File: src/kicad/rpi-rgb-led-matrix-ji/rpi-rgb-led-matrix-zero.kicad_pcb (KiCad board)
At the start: 2 copper layers, 65 x 30 mm, 11 parts, among them J1 Conn_01x02_Male, J2 Conn_02x10_Odd_Even, P1 Raspberry_Pi_2_3

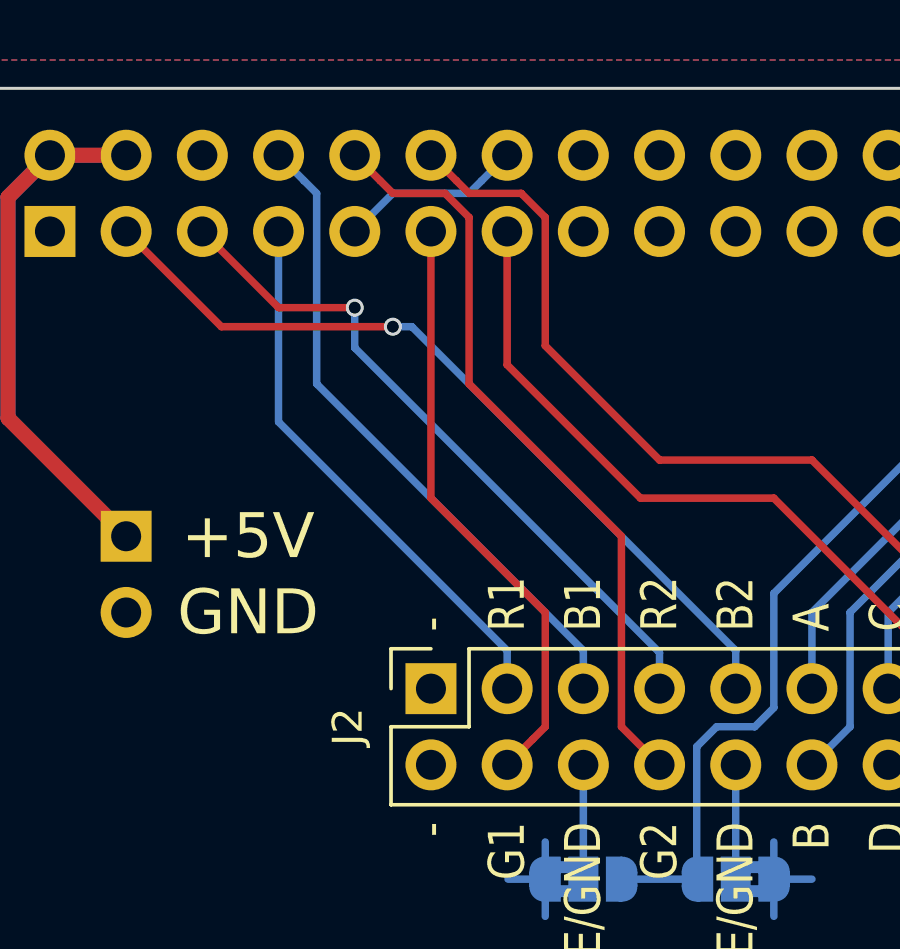
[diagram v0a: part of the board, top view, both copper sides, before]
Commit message: fixed g1/g2 inversion, removed virtual diode bypass
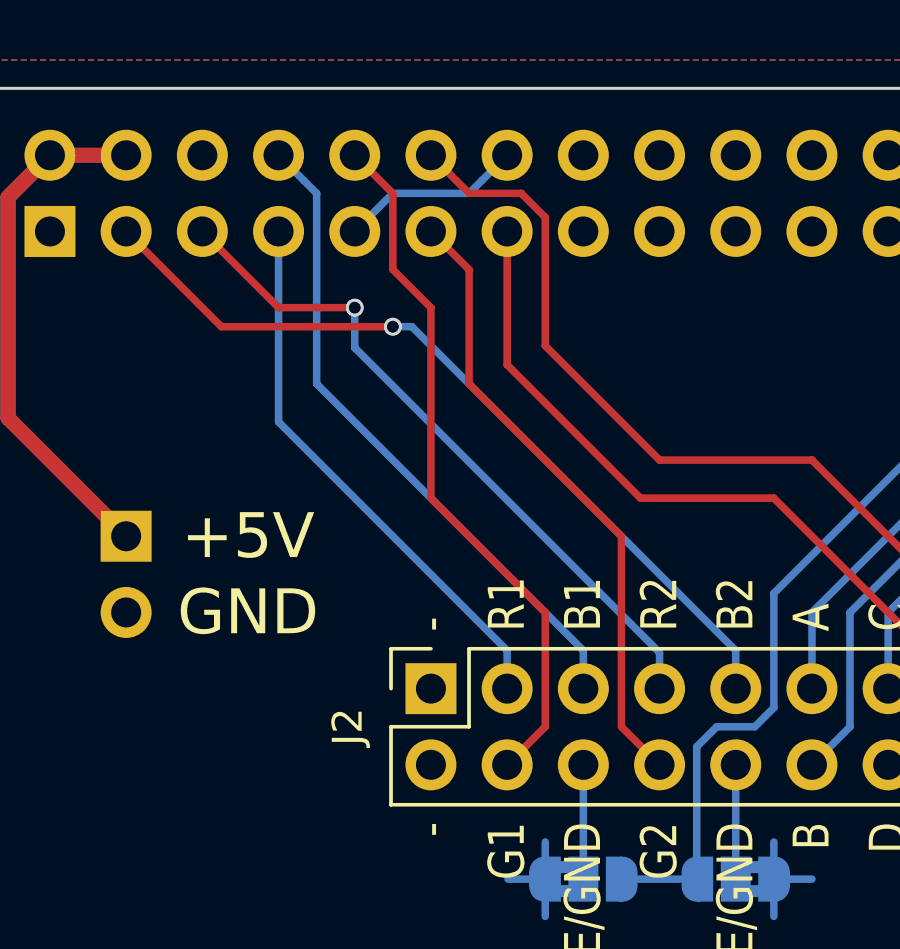
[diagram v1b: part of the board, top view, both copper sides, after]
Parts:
- H1, H2: value Power cable tie-down -> MountingHole
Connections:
- P1 pad 10: /G2_1 -> /G1_1
- P1 pad 11: /G1_1 -> /G2_1
- P1 pad 21: /G1_2 -> /G2_2
- P1 pad 22: /G2_2 -> /G1_2
- P1 pad 31: /G1_3 -> /G2_3
- P1 pad 32: /G2_3 -> /G1_3
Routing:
- net /G2_1: track 25.5 -> 20.9 mm
- net /G1_1: track 19.9 -> 23.5 mm
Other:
- board text added: "v1.2.3 20190324"
- board text removed: "v1.2 20190313"
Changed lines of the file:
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@@
     (thickness 1.6)
     (drawings 41)
-    (tracks 111)
+    (tracks 110)
     (zones 0)
     (modules 11)
@@
       (net 29 /E))
     (pad 32 thru_hole oval (at -2.54 -38.1 270) (size 1.7 1.7) (drill 1) (layers *.Cu *.Mask)
+      (net 30 /G1_3))
+    (pad 31 thru_hole oval (at 0 -38.1 270) (size 1.7 1.7) (drill 1) (layers *.Cu *.Mask)
       (net 28 /G2_3))
-    (pad 31 thru_hole oval (at 0 -38.1 270) (size 1.7 1.7) (drill 1) (layers *.Cu *.Mask)
-      (net 30 /G1_3))
     (pad 30 thru_hole oval (at -2.54 -35.56 270) (size 1.7 1.7) (drill 1) (layers *.Cu *.Mask)
       (net 1 GND))
@@
       (net 21 /B2_3))
     (pad 22 thru_hole oval (at -2.54 -25.4 270) (size 1.7 1.7) (drill 1) (layers *.Cu *.Mask)
+      (net 22 /G1_2))
+    (pad 21 thru_hole oval (at 0 -25.4 270) (size 1.7 1.7) (drill 1) (layers *.Cu *.Mask)
       (net 20 /G2_2))
-    (pad 21 thru_hole oval (at 0 -25.4 270) (size 1.7 1.7) (drill 1) (layers *.Cu *.Mask)
-      (net 22 /G1_2))
     (pad 20 thru_hole oval (at -2.54 -22.86 270) (size 1.7 1.7) (drill 1) (layers *.Cu *.Mask)
       (net 1 GND))
@@
       (net 14 /~OE))
     (pad 11 thru_hole oval (at 0 -12.7 270) (size 1.7 1.7) (drill 1) (layers *.Cu *.Mask)
+      (net 11 /G2_1))
+    (pad 10 thru_hole oval (at -2.54 -10.16 270) (size 1.7 1.7) (drill 1) (layers *.Cu *.Mask)
       (net 8 /G1_1))
-    (pad 10 thru_hole oval (at -2.54 -10.16 270) (size 1.7 1.7) (drill 1) (layers *.Cu *.Mask)
-      (net 11 /G2_1))
     (pad 9 thru_hole oval (at 0 -10.16 270) (size 1.7 1.7) (drill 1) (layers *.Cu *.Mask)
       (net 1 GND))
@@
       (effects (font (size 1 1) (thickness 0.15)))
     )
-    (fp_text value "Power cable tie-down" (at 0 -2.667 90) (layer F.Fab) hide
+    (fp_text value MountingHole (at 0 -2.667 90) (layer F.Fab) hide
       (effects (font (size 1 1) (thickness 0.15)))
     )
@@
       (effects (font (size 1 1) (thickness 0.15)))
     )
-    (fp_text value "Power cable tie-down" (at 0 -2.667 90) (layer F.Fab) hide
+    (fp_text value MountingHole (at 0 -2.667 90) (layer F.Fab) hide
       (effects (font (size 1 1) (thickness 0.15)))
     )
@@
     (effects (font (size 1.5 1.5) (thickness 0.3)) (justify mirror))
   )
-  (gr_text "v1.2 20190313" (at 16.51 5.715) (layer B.SilkS)
+  (gr_text "v1.2.3 20190324" (at 16.51 5.715) (layer B.SilkS)
     (effects (font (size 1.5 1.5) (thickness 0.3)) (justify mirror))
   )
@@
   (segment (start 7.62 6.35) (end 7.62 0) (width 0.25) (layer B.Cu) (net 7))
   (segment (start 15.24 13.97) (end 7.62 6.35) (width 0.25) (layer B.Cu) (net 7))
-  (segment (start 16.089999 16.930001) (end 15.24 17.78) (width 0.25) (layer F.Cu) (net 8))
-  (segment (start 16.51 16.51) (end 16.089999 16.930001) (width 0.25) (layer F.Cu) (net 8))
-  (segment (start 16.51 12.7) (end 16.51 16.51) (width 0.25) (layer F.Cu) (net 8))
-  (segment (start 12.7 0) (end 12.7 8.89) (width 0.25) (layer F.Cu) (net 8))
-  (segment (start 12.7 8.89) (end 16.51 12.7) (width 0.25) (layer F.Cu) (net 8))
+  (segment (start 11.43 -1.27) (end 10.16 -2.54) (width 0.25) (layer F.Cu) (net 8))
+  (segment (start 16.51 16.51) (end 16.51 12.7) (width 0.25) (layer F.Cu) (net 8))
+  (segment (start 15.24 17.78) (end 16.51 16.51) (width 0.25) (layer F.Cu) (net 8))
+  (segment (start 16.51 12.7) (end 12.7 8.89) (width 0.25) (layer F.Cu) (net 8))
+  (segment (start 12.7 8.89) (end 12.7 2.54) (width 0.25) (layer F.Cu) (net 8))
+  (segment (start 11.43 1.27) (end 11.43 -1.27) (width 0.25) (layer F.Cu) (net 8))
+  (segment (start 12.7 2.54) (end 11.43 1.27) (width 0.25) (layer F.Cu) (net 8))
   (segment (start 8.469999 -1.690001) (end 7.62 -2.54) (width 0.25) (layer B.Cu) (net 9))
   (segment (start 8.89 -1.27) (end 8.469999 -1.690001) (width 0.25) (layer B.Cu) (net 9))
@@
   (segment (start 7.62 2.54) (end 10.16 2.54) (width 0.25) (layer F.Cu) (net 10))
   (segment (start 5.08 0) (end 7.62 2.54) (width 0.25) (layer F.Cu) (net 10))
-  (segment (start 11.009999 -1.690001) (end 10.16 -2.54) (width 0.25) (layer F.Cu) (net 11))
-  (segment (start 11.43 -1.27) (end 11.009999 -1.690001) (width 0.25) (layer F.Cu) (net 11))
+  (segment (start 19.05 10.16) (end 13.97 5.08) (width 0.25) (layer F.Cu) (net 11))
   (segment (start 20.32 17.78) (end 19.05 16.51) (width 0.25) (layer F.Cu) (net 11))
-  (segment (start 19.05 10.16) (end 13.97 5.08) (width 0.25) (layer F.Cu) (net 11))
   (segment (start 19.05 16.51) (end 19.05 10.16) (width 0.25) (layer F.Cu) (net 11))
-  (segment (start 13.97 5.08) (end 13.97 -0.469002) (width 0.25) (layer F.Cu) (net 11))
-  (segment (start 13.97 -0.469002) (end 13.169002 -1.27) (width 0.25) (layer F.Cu) (net 11))
-  (segment (start 13.169002 -1.27) (end 11.43 -1.27) (width 0.25) (layer F.Cu) (net 11))
+  (segment (start 13.97 1.27) (end 12.7 0) (width 0.25) (layer F.Cu) (net 11))
+  (segment (start 13.97 5.08) (end 13.97 1.27) (width 0.25) (layer F.Cu) (net 11))
   (segment (start 22.86 15.24) (end 22.86 13.97) (width 0.25) (layer B.Cu) (net 12))
   (segment (start 22.86 13.97) (end 12.065 3.175) (width 0.25) (layer B.Cu) (net 12))
